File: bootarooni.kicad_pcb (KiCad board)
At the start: 2 copper layers, 25 parts, among them J1 USB_B_Micro, U1 74LS05, U2 Pico_USB, U3 ADUM3160, U4 74LCX541, U5 74AHCT1G125, U6 74LS299, U7 74LS299, U8 74LS299

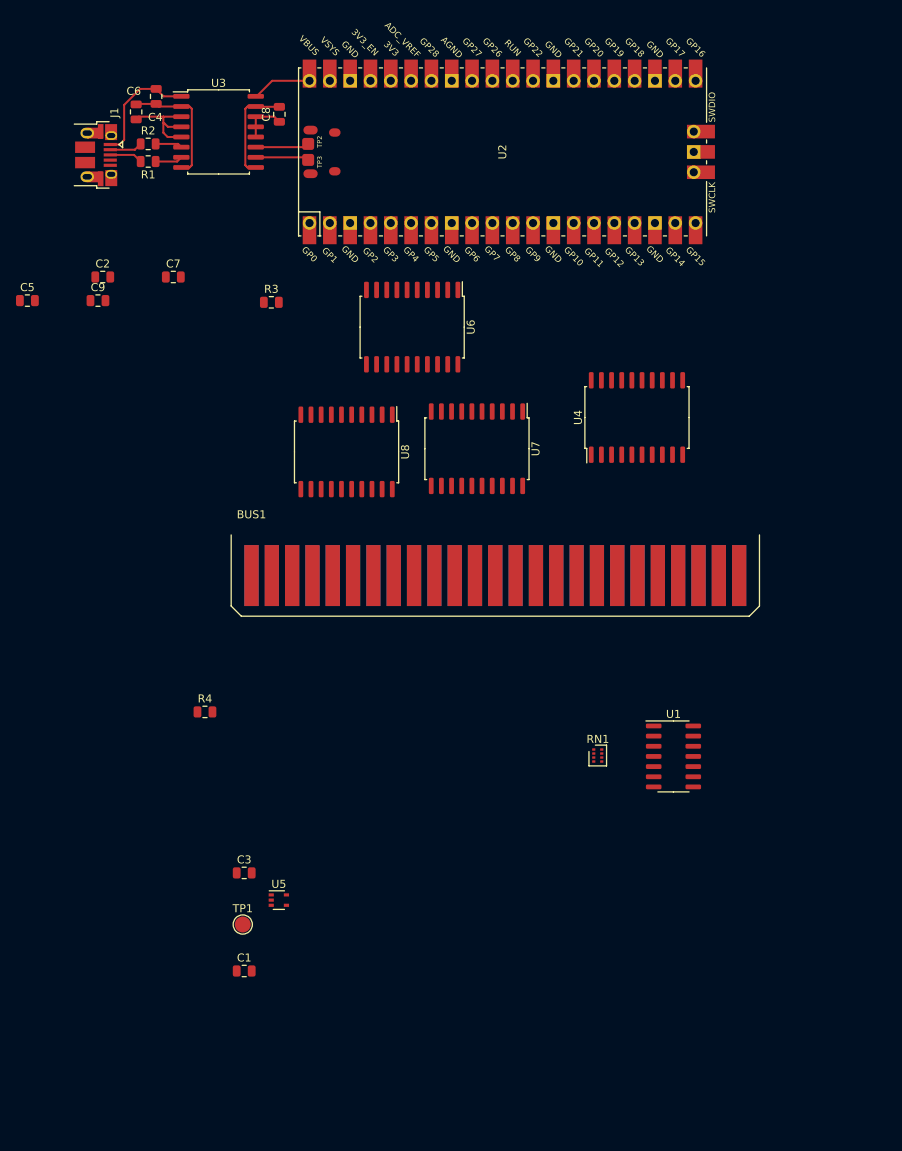
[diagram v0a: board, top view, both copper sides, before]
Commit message: added LEDs, most layout done, need to reroute the power line
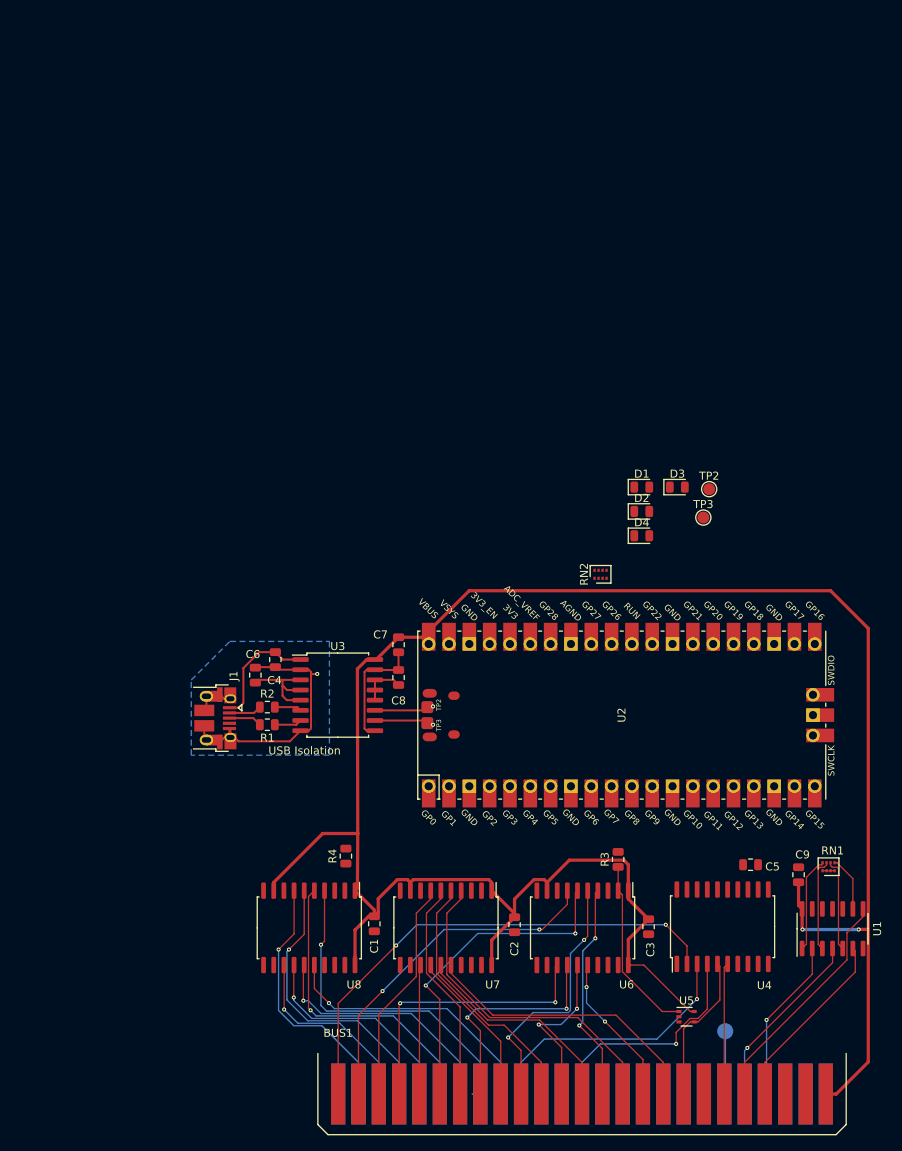
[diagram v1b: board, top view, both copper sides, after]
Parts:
- removed the C9 at (73.4, 10.5)
- added C7: 0.1uF, Capacitor_SMD:C_0805_2012Metric, F.Cu at (111.0, 53.5)
- added D1: GREEN, LED_SMD:LED_0805_2012Metric, F.Cu at (141.4, 33.8)
- added D2: GREEN, LED_SMD:LED_0805_2012Metric, F.Cu at (141.4, 36.8)
- added D3: GREEN, LED_SMD:LED_0805_2012Metric, F.Cu at (145.8, 33.8)
- added D4: GREEN, LED_SMD:LED_0805_2012Metric, F.Cu at (141.4, 39.9)
- added RN2: 470R, bootarooni:SOIC-8, F.Cu at (136.2, 44.7)
- added TP2: TestPoint, TestPoint:TestPoint_Pad_D1.5mm, F.Cu at (149.8, 34.1)
- added TP3: TestPoint, TestPoint:TestPoint_Pad_D1.5mm, F.Cu at (149.1, 37.6)
- TP1: moved to B.Cu
- moved C5 114.6 mm to (155.0, 81.0), turned to 180 degrees
- moved C9 108.1 mm to (161.0, 82.2), turned to 270 degrees
- moved C2 95.9 mm to (125.5, 88.5), turned to 90 degrees
- moved R3 82.0 mm to (138.4, 80.3), turned to 90 degrees
- moved U6 78.1 mm to (134.0, 88.9)
- moved C8 72.0 mm to (111.0, 57.6)
- moved J1 72.0 mm to (88.1, 62.7)
- moved R1 72.0 mm to (94.6, 63.5)
- moved C4 72.0 mm to (95.6, 55.4)
- moved C6 72.0 mm to (93.1, 57.3)
- moved R2 72.0 mm to (94.6, 61.3)
- moved U2 72.0 mm to (138.9, 62.3)
- moved U3 72.0 mm to (103.4, 59.8)
- moved BUS1 65.7 mm to (126.3, 109.7)
- moved U4 64.5 mm to (151.5, 88.8)
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- renumbered C7 to C9
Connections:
- net /ϕ1 renamed /PHI_1
- C5 pad 2: +5V -> +3V3
- R3 pad 1: Net-(R3-Pad1) -> /ADDR_~OE~
- R4 pad 1: Net-(R4-Pad1) -> /DATA_~OE~
- RN1 pad 5: Net-(RN1-Pad5) -> /P_RDY
- RN1 pad 6: Net-(RN1-Pad6) -> /P_~DMA~
- RN1 pad 7: Net-(RN1-Pad7) -> /P_~IRQ~
- RN1 pad 8: Net-(RN1-Pad8) -> /P_~NMI~
- U1 pad 1: Net-(RN1-Pad8) -> /P_~NMI~
- U1 pad 10: (no net) -> Net-(U1-Pad10)
- U1 pad 11: (no net) -> GND
- U1 pad 12: (no net) -> Net-(U1-Pad12)
- U1 pad 13: (no net) -> GND
- U1 pad 3: Net-(RN1-Pad7) -> /P_~IRQ~
- U1 pad 5: Net-(RN1-Pad6) -> /P_~DMA~
- U1 pad 9: Net-(RN1-Pad5) -> /P_RDY
- U2 pad 1: Net-(U2-Pad1) -> /DATA_IN
- U2 pad 10: Net-(U2-Pad10) -> /ADDR_FN
- U2 pad 11: Net-(U2-Pad11) -> /ADDR_EVEN_IN
- U2 pad 12: Net-(U2-Pad12) -> /P_~IOSEL~
- U2 pad 14: Net-(U2-Pad14) -> /P_~DEVSEL~
- U2 pad 15: Net-(U2-Pad15) -> /P_ϕ1
- U2 pad 16: Net-(U2-Pad16) -> /P_R_~W~
- U2 pad 17: Net-(U2-Pad17) -> /P_D_OUT
- U2 pad 19: Net-(U2-Pad19) -> /P_AO_OUT
- U2 pad 2: Net-(U2-Pad2) -> /DATA_CLK
- U2 pad 20: Net-(U2-Pad20) -> /P_AE_OUT
- U2 pad 21: Net-(U2-Pad21) -> /P_RDY
- U2 pad 22: Net-(U2-Pad22) -> /P_~DMA~
- U2 pad 24: Net-(U2-Pad24) -> /P_~IRQ~
- U2 pad 25: Net-(U2-Pad25) -> /P_~NMI~
- U2 pad 26: Net-(U2-Pad26) -> /P_~STROBE~
- U2 pad 27: Net-(U2-Pad27) -> /P_R_~W~_OUT
- U2 pad 4: Net-(U2-Pad4) -> /DATA_~OE~
- U2 pad 42: Net-(U2-Pad42) -> GND
- U2 pad 5: Net-(U2-Pad5) -> /DATA_FN
- U2 pad 6: Net-(U2-Pad6) -> /ADDR_ODD_IN
- U2 pad 7: Net-(U2-Pad7) -> /ADDR_CLK
- U2 pad 9: Net-(U2-Pad9) -> /ADDR_~OE~
- U4 pad 11: Net-(U4-Pad11) -> /P_AE_OUT
- U4 pad 12: Net-(U4-Pad12) -> /P_AO_OUT
- U4 pad 13: Net-(U4-Pad13) -> /P_D_OUT
- U4 pad 14: Net-(U4-Pad14) -> /P_~STROBE~
- U4 pad 15: Net-(U4-Pad15) -> /P_R_~W~
- U4 pad 16: Net-(U4-Pad16) -> /P_ϕ1
- U4 pad 17: Net-(U4-Pad17) -> /P_~DEVSEL~
- U4 pad 18: Net-(U4-Pad18) -> /P_~IOSEL~
- U4 pad 7: GND -> /DATA_OUT
- U4 pad 8: GND -> /ADDR_ODD_OUT
- U4 pad 9: GND -> /ADDR_EVEN_OUT
- U5 pad 1: Net-(R3-Pad1) -> /ADDR_~OE~
- U5 pad 2: Net-(U5-Pad2) -> /P_R_~W~_OUT
- U6 pad 11: Net-(U6-Pad11) -> /ADDR_EVEN_IN
- U6 pad 12: Net-(U6-Pad12) -> /ADDR_CLK
- U6 pad 17: Net-(U6-Pad17) -> /ADDR_EVEN_OUT
- U6 pad 19: Net-(U6-Pad19) -> /ADDR_FN
- U6 pad 2: Net-(R3-Pad1) -> /ADDR_~OE~
- U7 pad 11: Net-(U7-Pad11) -> /ADDR_ODD_IN
- U7 pad 12: Net-(U6-Pad12) -> /ADDR_CLK
- U7 pad 17: Net-(U7-Pad17) -> /ADDR_ODD_OUT
- U7 pad 19: Net-(U6-Pad19) -> /ADDR_FN
- U7 pad 2: Net-(R3-Pad1) -> /ADDR_~OE~
- U8 pad 11: Net-(U8-Pad11) -> /DATA_IN
- U8 pad 12: Net-(U8-Pad12) -> /DATA_CLK
- U8 pad 17: Net-(U8-Pad17) -> /DATA_OUT
- U8 pad 19: Net-(U8-Pad19) -> /DATA_FN
- U8 pad 2: Net-(R4-Pad1) -> /DATA_~OE~
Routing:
- net +5V: track 7.53 -> 282.2 mm, vias 0 -> 2
- net /~IOSEL~: track 0.00 -> 62.3 mm, vias 0 -> 2
- net /A0: track 0.00 -> 43.4 mm, vias 0 -> 2
- net /D6: track 0.00 -> 42.4 mm, vias 0 -> 1
- net /A13: track 0.00 -> 41.7 mm
- net /A4: track 0.00 -> 41.2 mm, vias 0 -> 2
- net /D4: track 0.00 -> 38.2 mm, vias 0 -> 1
- net /A15: track 0.00 -> 36.1 mm
- net /D2: track 0.00 -> 35.8 mm, vias 0 -> 1
- net /A2: track 0.00 -> 35.6 mm, vias 0 -> 2
- net /D7: track 0.00 -> 34.0 mm, vias 0 -> 1
- net /~DEVSEL~: track 0.00 -> 33.6 mm, vias 0 -> 1
- net /D0: track 0.00 -> 32.9 mm, vias 0 -> 1
- net /A8: track 0.00 -> 32.8 mm, vias 0 -> 2
- net /A9: track 0.00 -> 32.7 mm
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- added copper zone on B.Cu, net /EXT_GND
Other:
- board text added: "USB Isolation"

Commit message: initial layout done, needs board edge and mounting holes, along with verification
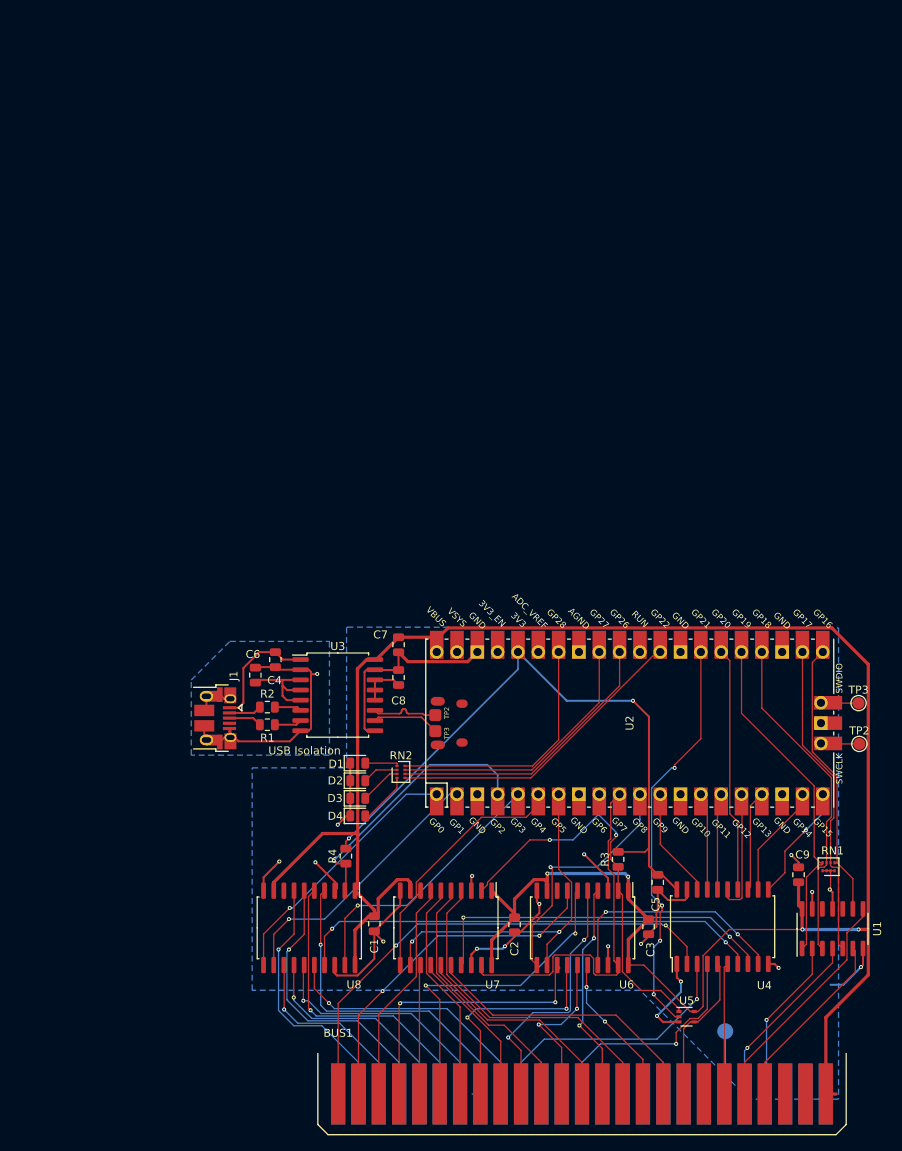
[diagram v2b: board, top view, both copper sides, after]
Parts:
- moved D3 55.8 mm to (105.9, 72.7)
- moved D4 49.9 mm to (105.9, 74.9)
- moved D1 49.5 mm to (105.9, 68.3)
- moved D2 48.9 mm to (105.9, 70.5)
- moved TP2 37.0 mm to (168.6, 65.9)
- moved RN2 35.1 mm to (111.3, 69.4), turned to 270 degrees
- moved TP3 30.2 mm to (168.5, 60.8)
- moved C5 11.8 mm to (143.4, 83.2), turned to 90 degrees
- moved U2 1.41 mm to (139.9, 63.3)
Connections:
- net /USB_DM renamed /USB_D-
- net /USB_DP renamed /USB_D+
- RN2 pad 1: Net-(RN2-Pad1) -> Net-(D1-Pad2)
- RN2 pad 2: Net-(RN2-Pad2) -> Net-(D2-Pad2)
- RN2 pad 3: Net-(RN2-Pad3) -> Net-(D3-Pad2)
- RN2 pad 4: Net-(RN2-Pad4) -> Net-(D4-Pad2)
- RN2 pad 5: Net-(D4-Pad2) -> Net-(RN2-Pad5)
- RN2 pad 6: Net-(D3-Pad2) -> Net-(RN2-Pad6)
- RN2 pad 7: Net-(D2-Pad2) -> Net-(RN2-Pad7)
- RN2 pad 8: Net-(D1-Pad2) -> Net-(RN2-Pad8)
- U2 pad 29: Net-(RN2-Pad4) -> Net-(RN2-Pad5)
- U2 pad 31: Net-(RN2-Pad3) -> Net-(RN2-Pad6)
- U2 pad 32: Net-(RN2-Pad2) -> Net-(RN2-Pad7)
- U2 pad 34: Net-(RN2-Pad1) -> Net-(RN2-Pad8)
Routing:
- net GND: track 16.5 -> 131.2 mm, vias 0 -> 18
- net +3V3: track 0.00 -> 81.1 mm, vias 0 -> 2
- net /DATA_OUT: track 0.00 -> 58.9 mm, vias 0 -> 2
- net /P_R_~W~_OUT: track 0.00 -> 50.9 mm, vias 0 -> 4
- net /ADDR_FN: track 0.00 -> 46.0 mm
- net /ADDR_CLK: track 0.00 -> 45.2 mm, vias 0 -> 2
- net /ADDR_ODD_OUT: track 0.00 -> 44.7 mm, vias 0 -> 2
- net Net-(RN2-Pad5): track 0.00 -> 38.4 mm
- net Net-(RN2-Pad6): track 0.00 -> 35.6 mm
- net Net-(RN2-Pad7): track 0.00 -> 34.1 mm
- net /DATA_CLK: track 0.00 -> 34.0 mm, vias 0 -> 1
- net /DATA_FN: track 0.00 -> 33.9 mm, vias 0 -> 1
- net /DATA_~OE~: track 0.00 -> 33.5 mm, vias 0 -> 1
- net /DATA_IN: track 0.00 -> 32.8 mm, vias 0 -> 1
- net /ADDR_ODD_IN: track 0.00 -> 31.8 mm
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- added copper zone on B.Cu, net GND
